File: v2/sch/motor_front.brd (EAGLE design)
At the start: 93 x 31.6 mm, 6 parts

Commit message: routing almost finished
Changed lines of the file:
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@@
 </class>
 </classes>
-<designrules name="default">
-<description language="de">&lt;b&gt;EAGLE Design Rules&lt;/b&gt;
-&lt;p&gt;
-Die Standard-Design-Rules sind so gewählt, dass sie für
-die meisten Anwendungen passen. Sollte ihre Platine
-besondere Anforderungen haben, treffen Sie die erforderlichen
-Einstellungen hier und speichern die Design Rules unter
-einem neuen Namen ab.</description>
-<description language="en">&lt;b&gt;EAGLE Design Rules&lt;/b&gt;
-&lt;p&gt;
-The default Design Rules have been set to cover
-a wide range of applications. Your particular design
-may have different requirements, so please make the
-necessary adjustments and save your customized
-design rules under a new name.</description>
+<designrules name="jlcpcb-2layers">
+<description language="en">&lt;b&gt;JLCPCB design rules (2 layers)&lt;/b&gt;
+&lt;ul&gt;
+&lt;li&gt;Board thickness: 1.6mm&lt;/li&gt;
+&lt;li&gt;Copper weight: 1oz (35um)&lt;/li&gt;
+&lt;li&gt;Note: annular ring aren't minimal&lt;/li&gt;
+&lt;/ul&gt;</description>
 <param name="layerSetup" value="(1*16)"/>
 <param name="mtCopper" value="0.035mm 0.035mm 0.035mm 0.035mm 0.035mm 0.035mm 0.035mm 0.035mm 0.035mm 0.035mm 0.035mm 0.035mm 0.035mm 0.035mm 0.035mm 0.035mm"/>
-<param name="mtIsolate" value="1.5mm 0.15mm 0.2mm 0.15mm 0.2mm 0.15mm 0.2mm 0.15mm 0.2mm 0.15mm 0.2mm 0.15mm 0.2mm 0.15mm 0.2mm"/>
-<param name="mdWireWire" value="8mil"/>
-<param name="mdWirePad" value="8mil"/>
-<param name="mdWireVia" value="8mil"/>
-<param name="mdPadPad" value="8mil"/>
-<param name="mdPadVia" value="8mil"/>
-<param name="mdViaVia" value="8mil"/>
-<param name="mdSmdPad" value="8mil"/>
-<param name="mdSmdVia" value="8mil"/>
-<param name="mdSmdSmd" value="8mil"/>
-<param name="mdViaViaSameLayer" value="8mil"/>
+<param name="mtIsolate" value="1.6mm 0.15mm 0.2mm 0.15mm 0.2mm 0.15mm 0.2mm 0.15mm 0.2mm 0.15mm 0.2mm 0.15mm 0.2mm 0.15mm 0.2mm"/>
+<param name="mdWireWire" value="5mil"/>
+<param name="mdWirePad" value="5mil"/>
+<param name="mdWireVia" value="5mil"/>
+<param name="mdPadPad" value="5mil"/>
+<param name="mdPadVia" value="5mil"/>
+<param name="mdViaVia" value="5mil"/>
+<param name="mdSmdPad" value="5mil"/>
+<param name="mdSmdVia" value="5mil"/>
+<param name="mdSmdSmd" value="5mil"/>
+<param name="mdViaViaSameLayer" value="6mil"/>
 <param name="mnLayersViaInSmd" value="2"/>
-<param name="mdCopperDimension" value="40mil"/>
-<param name="mdDrill" value="8mil"/>
+<param name="mdCopperDimension" value="0.2mm"/>
+<param name="mdDrill" value="6mil"/>
 <param name="mdSmdStop" value="0mil"/>
-<param name="msWidth" value="10mil"/>
-<param name="msDrill" value="24mil"/>
-<param name="msMicroVia" value="9.99mm"/>
+<param name="msWidth" value="5mil"/>
+<param name="msDrill" value="0.3mm"/>
+<param name="msMicroVia" value="0.3mm"/>
 <param name="msBlindViaRatio" value="0.5"/>
-<param name="rvPadTop" value="0.25"/>
-<param name="rvPadInner" value="0.25"/>
-<param name="rvPadBottom" value="0.25"/>
-<param name="rvViaOuter" value="0.25"/>
-<param name="rvViaInner" value="0.25"/>
-<param name="rvMicroViaOuter" value="0.25"/>
-<param name="rvMicroViaInner" value="0.25"/>
+<param name="rvPadTop" value="0.4"/>
+<param name="rvPadInner" value="0"/>
+<param name="rvPadBottom" value="0.4"/>
+<param name="rvViaOuter" value="0"/>
+<param name="rvViaInner" value="0"/>
+<param name="rvMicroViaOuter" value="0"/>
+<param name="rvMicroViaInner" value="0"/>
 <param name="rlMinPadTop" value="10mil"/>
-<param name="rlMaxPadTop" value="20mil"/>
+<param name="rlMaxPadTop" value="80mil"/>
 <param name="rlMinPadInner" value="10mil"/>
 <param name="rlMaxPadInner" value="20mil"/>
 <param name="rlMinPadBottom" value="10mil"/>
-<param name="rlMaxPadBottom" value="20mil"/>
-<param name="rlMinViaOuter" value="8mil"/>
+<param name="rlMaxPadBottom" value="80mil"/>
+<param name="rlMinViaOuter" value="3mil"/>
 <param name="rlMaxViaOuter" value="20mil"/>
 <param name="rlMinViaInner" value="8mil"/>
 <param name="rlMaxViaInner" value="20mil"/>
-<param name="rlMinMicroViaOuter" value="4mil"/>
+<param name="rlMinMicroViaOuter" value="3mil"/>
 <param name="rlMaxMicroViaOuter" value="20mil"/>
 <param name="rlMinMicroViaInner" value="4mil"/>
@@
 </signal>
 </signals>
+<errors>
+</errors>
 </board>
 </drawing>

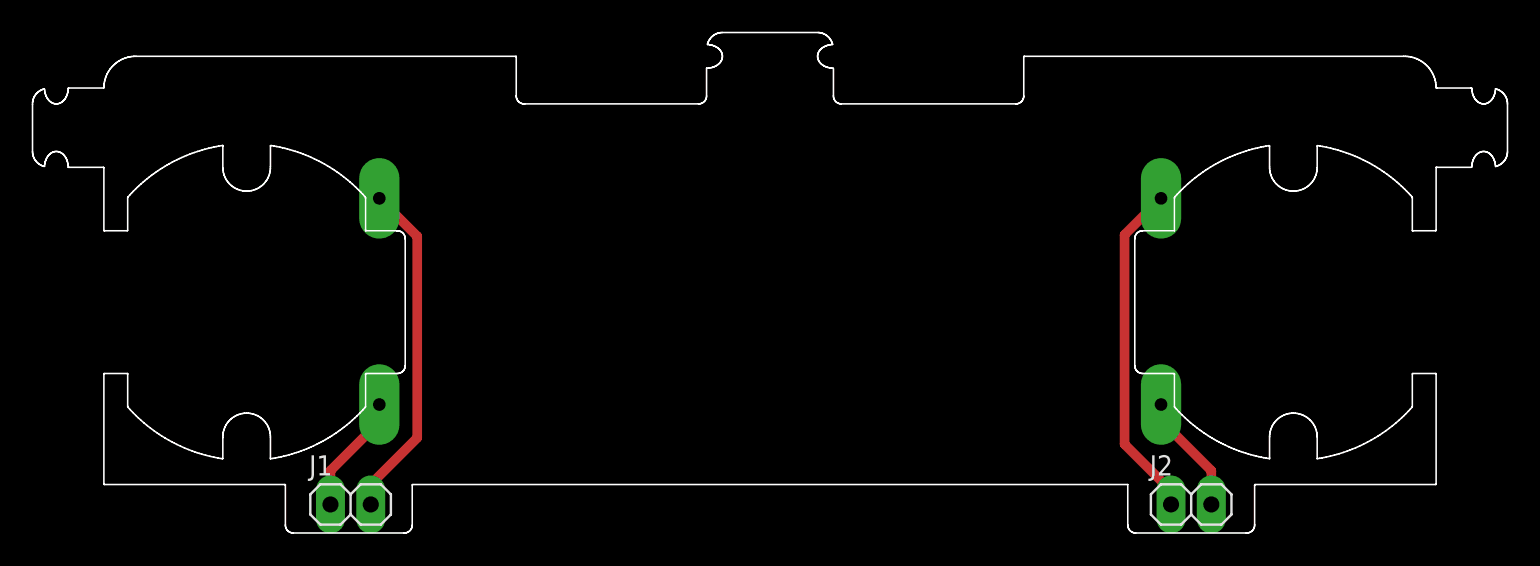
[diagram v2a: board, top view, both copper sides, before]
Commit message: add bumpers
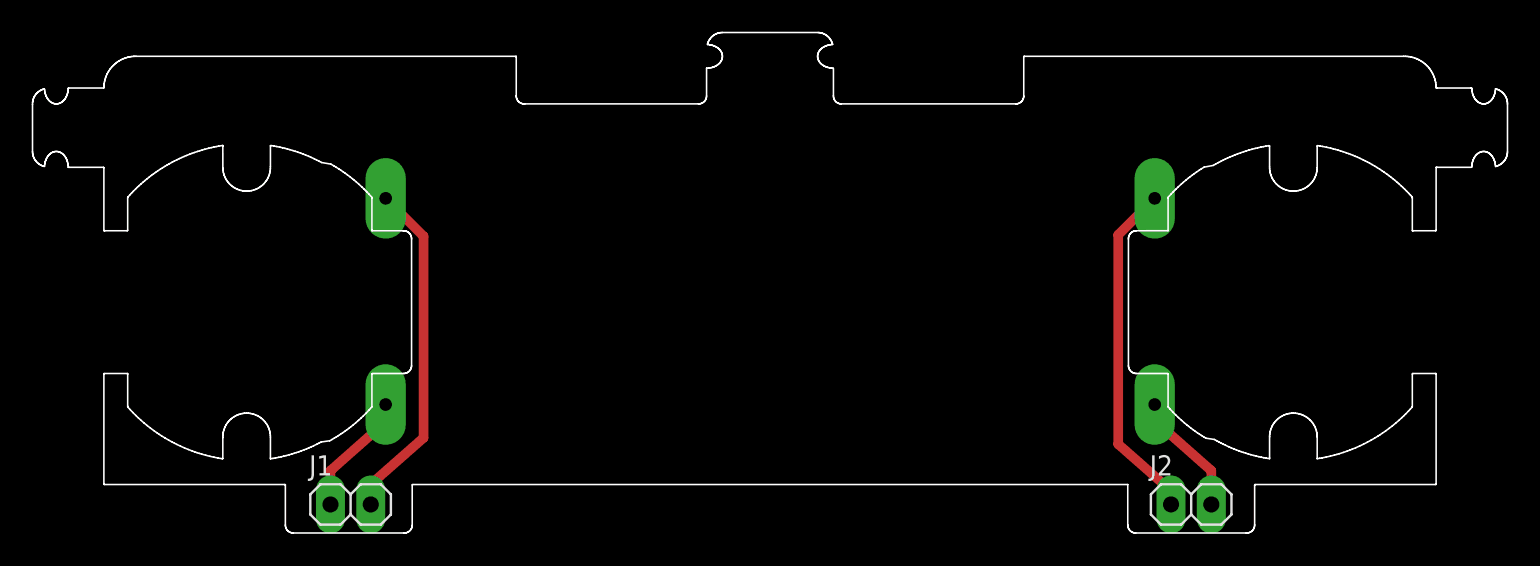
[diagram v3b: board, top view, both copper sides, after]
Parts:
- moved U$3 0.40 mm to (70.1, 8.10)
- moved U$4 0.40 mm to (70.1, 21.1)
- moved U$1 0.40 mm to (21.6, 8.10)
- moved U$2 0.40 mm to (21.6, 21.1)
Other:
- outline, holes or cut-outs redrawn
